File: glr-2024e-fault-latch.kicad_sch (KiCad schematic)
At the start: 110 parts, among them K101 Fujitsu_FTR-LYAA005x, K102 Fujitsu_FTR-LYAA005x, K103 Fujitsu_FTR-LYAA005x, Q101 Q_NPN_BEC, Q102 Q_NPN_BEC, Q103 Q_NPN_BEC, Q104 Q_NPN_BEC, Q105 Q_NMOS_GSD, Q106 Q_NMOS_GSD, Q107 Q_PMOS_GSD, Q108 Q_PMOS_GSD, Q109 Q_NMOS_GDS, Q110 Q_NPN_BEC, Q111 Q_NPN_BEC, Q112 Q_NMOS_GSD, Q113 Q_PMOS_GSD, Q114 Q_NMOS_GSD, Q115 Q_NMOS_GSD, SW101 SW_Omron_B3FS, SW102 SW_Omron_B3FS, SW103 SW_Omron_B3FS, U101 SFH617A-1, U102 SFH617A-1, U103 SFH617A-1, U104 74AHC1G00, U105 74AHC1G00, U106 74AHC1G00, U107 74LS279, U108 641964-1, U109 SFH617A-1, U110 SFH617A-1, U111 641964-1, U112 641964-1, U113 641964-1, U114 641964-1, U115 641964-1, U116 641964-1, U117 74AHC1G00, U118 LM555xM, U119 74AHC1G00, U120 641964-1, U121 SFH617A-1, U122 641964-1, U123 641964-1

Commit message: work in progress
keep only bms and imd
remove tssi stuff

Co-Authored-By: wallalex0 <97884125+wallalex0@users.noreply.github.com>
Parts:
- removed C104: 100n, Capacitor_SMD:C_0603_1608Metric_Pad1.08x0.95mm_HandSolder, symbol Device:C
- removed C106: 10n, Capacitor_SMD:C_0603_1608Metric_Pad1.08x0.95mm_HandSolder, symbol Device:C
- removed C107: 1u, Capacitor_SMD:C_0402_1005Metric, symbol Device:C_Polarized_US
- removed C108, C110, C112: 0.1u, Capacitor_SMD:C_0402_1005Metric, symbol Device:C
- removed C109: .01u, Capacitor_SMD:C_0402_1005Metric, symbol Device:C
- removed C111: 22u, Capacitor_SMD:C_0402_1005Metric, symbol Device:C
- removed D103: RED, LED_SMD:LED_0805_2012Metric_Pad1.15x1.40mm_HandSolder, symbol Device:LED
- removed D105, D107, D108: D_Schottky, Diode_SMD:D_SMA, symbol Device:D_Schottky
- removed K102: Fujitsu_FTR-LYAA005x, Relay_THT:Relay_SPST-NO_Fujitsu_FTR-LYAA005x_FormA_Vertical, symbol Relay:Fujitsu_FTR-LYAA005x
- removed Q109: Q_NMOS_GDS, Package_TO_SOT_SMD:TO-252-2, symbol Transistor_FET:Q_NMOS_GDS
- removed Q110, Q111: Q_NPN_BEC, Package_TO_SOT_SMD:SOT-23, symbol Transistor_BJT:Q_NPN_BEC
- removed Q112: Q_NMOS_GSD, Package_TO_SOT_SMD:SOT-23, symbol Transistor_FET:Q_NMOS_GSD
- removed Q113: Q_PMOS_GSD, Package_TO_SOT_SMD:SOT-523, symbol Transistor_FET:Q_PMOS_GSD
- removed R104, R107, R123: 10k, Resistor_SMD:R_0805_2012Metric_Pad1.20x1.40mm_HandSolder, symbol Device:R_US
- removed R118: 270R, Resistor_SMD:R_0805_2012Metric_Pad1.20x1.40mm_HandSolder, symbol Device:R_US
- removed R122, R127: 100k, Resistor_SMD:R_0805_2012Metric_Pad1.20x1.40mm_HandSolder, symbol Device:R_US
- removed R124, R129: 1k, Resistor_SMD:R_0805_2012Metric_Pad1.20x1.40mm_HandSolder, symbol Device:R_US
- removed R128, R133, R134: 10k, Resistor_SMD:R_0603_1608Metric, symbol Device:R_US
- removed R130: 270R, Resistor_SMD:R_0603_1608Metric, symbol Device:R_US
- removed R131: 15k, Resistor_SMD:R_0603_1608Metric, symbol Device:R_US
- removed R132: 100k, Resistor_SMD:R_0603_1608Metric, symbol Device:R_US
- removed SW103: SW_Omron_B3FS, Button_Switch_SMD:SW_SPST_Omron_B3FS-100xP, symbol Switch:SW_Omron_B3FS
- removed U103, U121: SFH617A-1, Package_DIP:DIP-4_W7.62mm, symbol Isolator:SFH617A-1
- removed U106, U117, U119: 74AHC1G00, Package_TO_SOT_SMD:SOT-23-5, symbol 74xGxx:74AHC1G00
- removed U111, U113, U114, U122: 641964-1, 641964-1:TE_641964-1, symbol CONNECTOR:641964-1
- removed U118: LM555xM, Package_SO:SOIC-8_3.9x4.9mm_P1.27mm, symbol Timer:LM555xM
- U101, U102, U107, U108, U109, U110, U112, U115, U116, U120, U123: now fitted
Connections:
- net +12V: no longer R102.2
- net GNDPWR: now also R102.1
- net BMS_INPUT: now reaches U101.1
- net BMS_INPUT: now also U115.1; no longer R102.1
- net SDC_IN: now reaches K103.13, U112.1
- net SDC: now reaches K103.14
- net SDC: now also K101.13; no longer U112.2
- net at U107.11 (~{S}): no longer U107.12 (~{S})
- net at U108.1: now also R112.2; no longer Q106.3 (D)
- net at U108.2: now also Q106.3 (D); no longer R112.2
- net SDC_OUT: now reaches K101.14
- net SDC_OUT: now also U112.2
- net at Q115.3 (D): now also U123.2; no longer U123.1
- net at R135.2: now also U123.1; no longer U123.2
- net BSPD_HV: no longer names the net of U116.2
- net IMD_HV renamed IMD_INPUT
- net NBMS_HV: no longer names the net of U101.2
- net NBMS_HV: now also R102.2; no longer U115.2
- net NBPSD_LV: no longer names the net of U107.10 (~{R})
- no-connect marks 5 -> 9
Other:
- note removed: "f = 1 / (0.693 * (2R106) * C102)"
- note removed: "https://www.electronics-tutorials.ws/waveforms/555_oscillator.html"
- moved on the sheet: C105, C113, C114, C115, C116, C117, D101, D106, H101, H102, H103, H104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

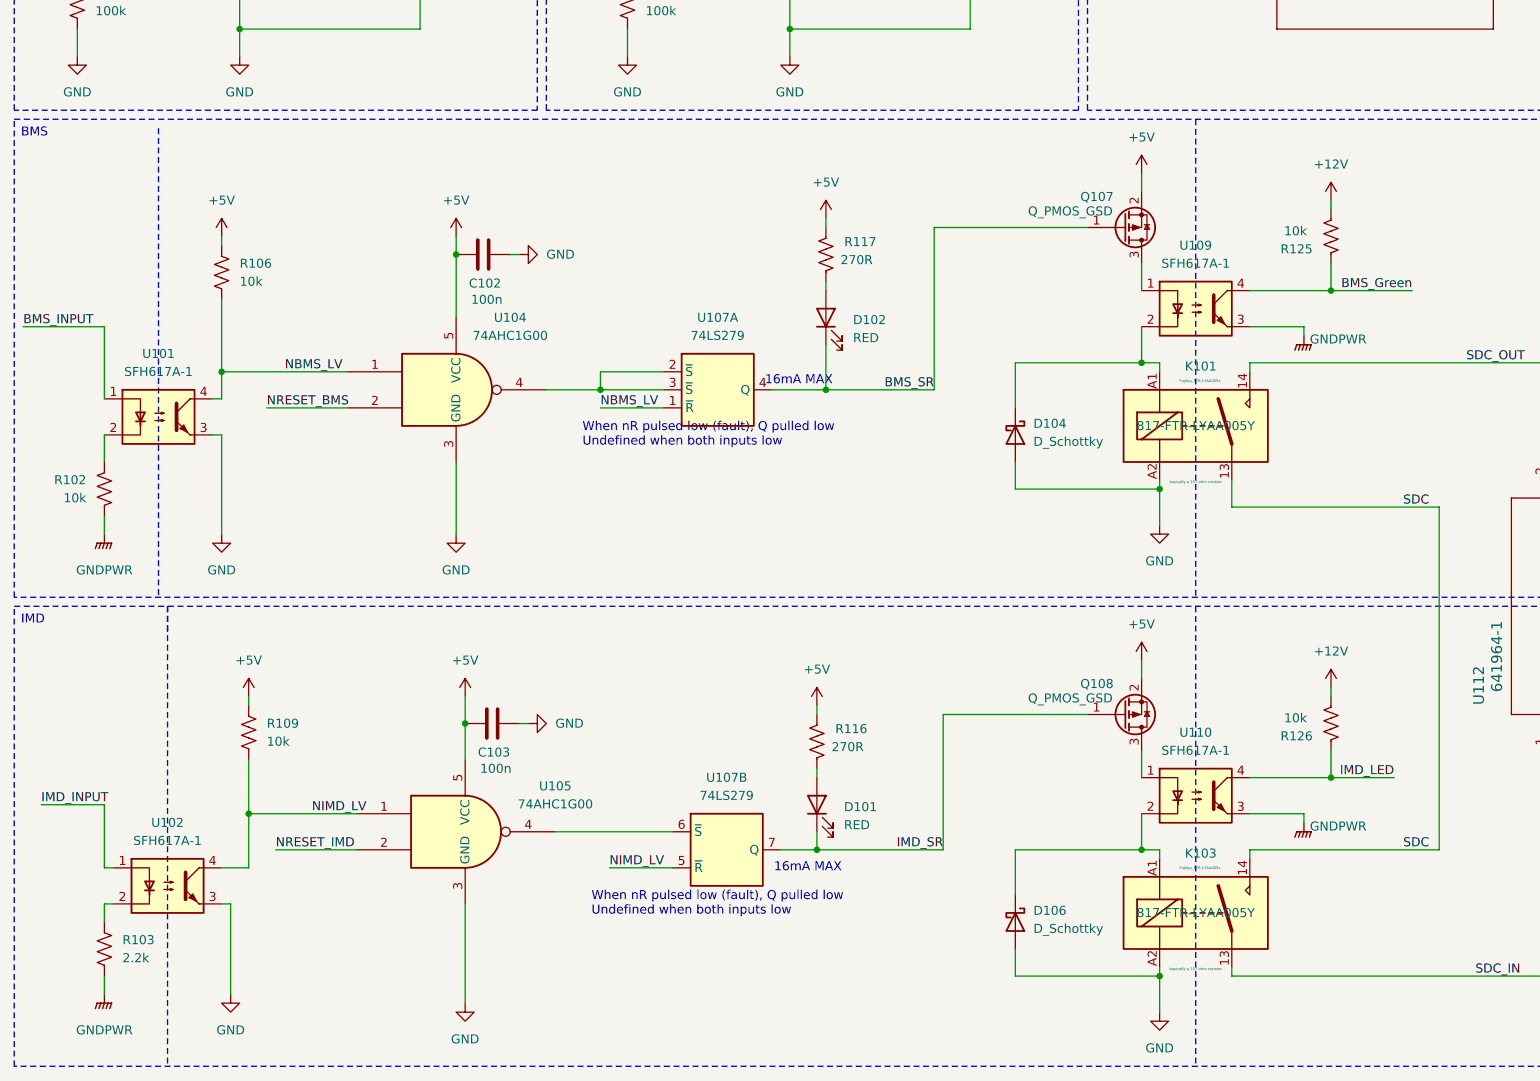
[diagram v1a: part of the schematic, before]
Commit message: almost finished
add bms light logic
improve overall placements of components
improve routing
improve silk component identifiers

Co-Authored-By: wallalex0 <97884125+wallalex0@users.noreply.github.com>
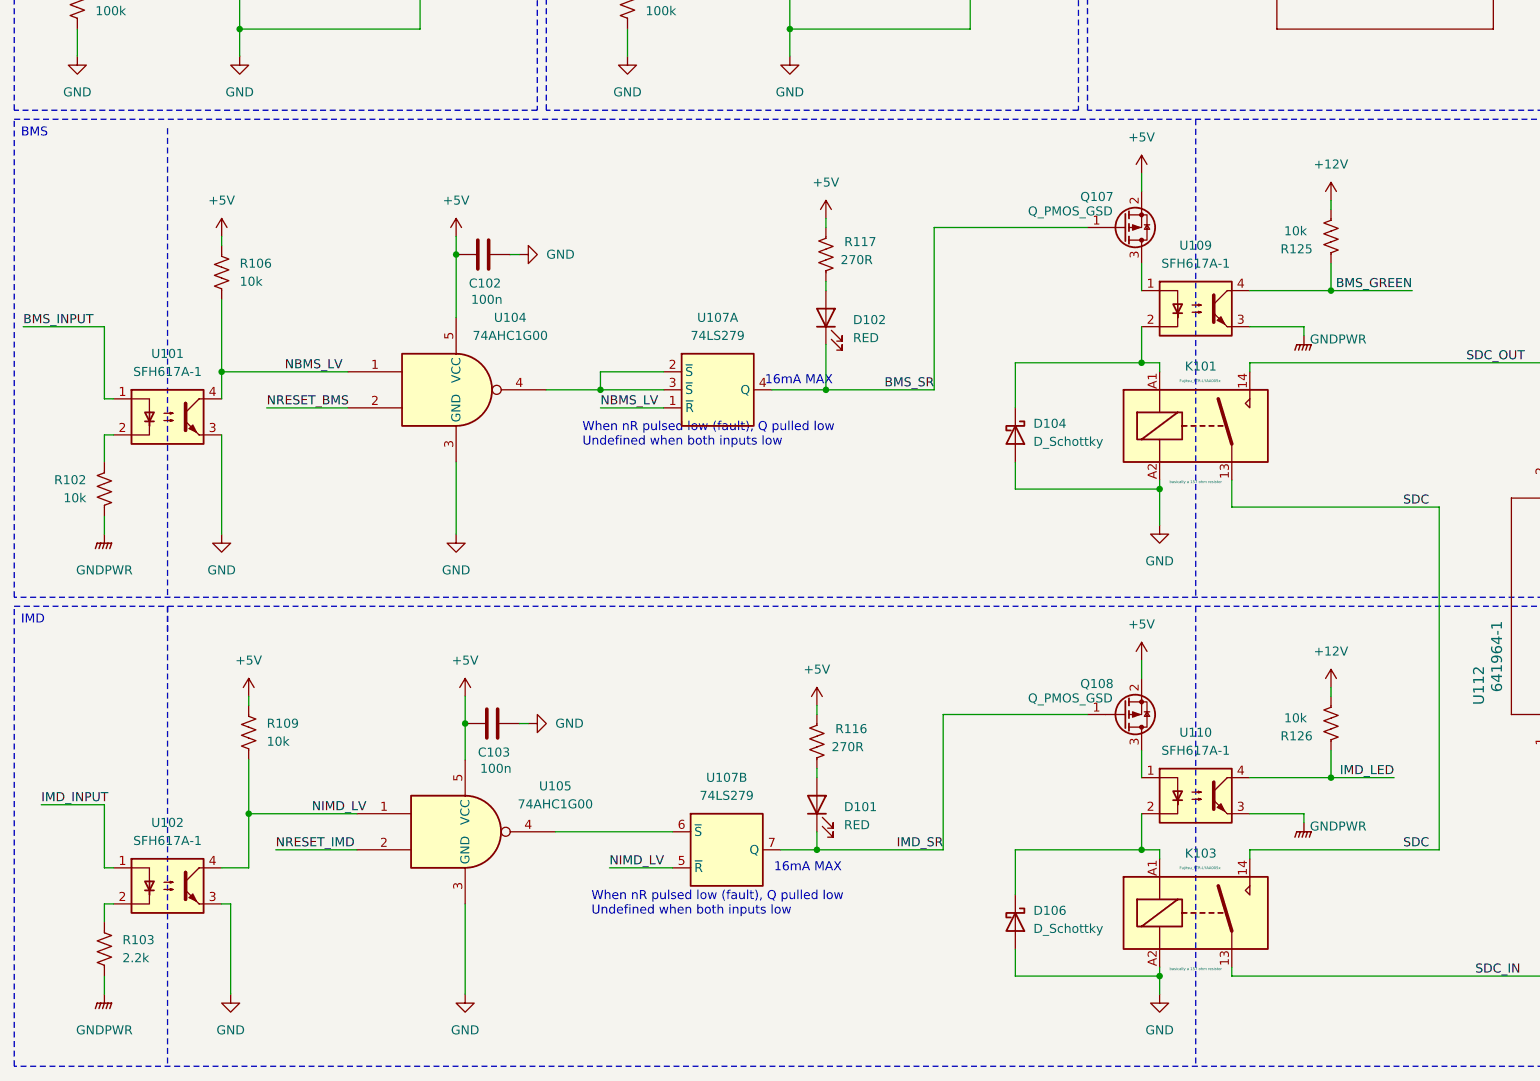
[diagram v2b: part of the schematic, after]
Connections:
- net BMS_Green is gone; now on net BMS_GREEN: R125.2, U109.4
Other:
- moved on the sheet: U101
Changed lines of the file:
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@@
 	(polyline
 		(pts
-			(xy 45.72 85.09) (xy 45.72 151.13)
+			(xy 46.99 85.09) (xy 46.99 151.13)
 		)
 		(stroke
@@
 	(wire
 		(pts
+			(xy 39.37 128.27) (xy 38.1 128.27)
+		)
+		(stroke
+			(width 0)
+			(type default)
+		)
+	)
+	(wire
+		(pts
 			(xy 308.61 125.73) (xy 308.61 115.57)
 		)
@@
 	(wire
 		(pts
-			(xy 53.34 128.27) (xy 54.61 128.27)
-		)
-		(stroke
-			(width 0)
-			(type default)
-		)
-	)
-	(wire
-		(pts
 			(xy 58.42 165.1) (xy 58.42 166.37)
 		)
@@
 	(wire
 		(pts
+			(xy 38.1 123.19) (xy 39.37 123.19)
+		)
+		(stroke
+			(width 0)
+			(type default)
+		)
+	)
+	(wire
+		(pts
 			(xy 276.86 113.03) (xy 288.29 113.03)
 		)
@@
 	(wire
 		(pts
-			(xy 186.69 204.47) (xy 186.69 209.55)
+			(xy 186.69 204.47) (xy 186.69 207.01)
 		)
 		(stroke
@@
 	(wire
 		(pts
+			(xy 38.1 128.27) (xy 38.1 132.08)
+		)
+		(stroke
+			(width 0)
+			(type default)
+		)
+	)
+	(wire
+		(pts
 			(xy 58.42 173.99) (xy 58.42 181.61)
 		)
@@
 	(wire
 		(pts
-			(xy 38.1 128.27) (xy 38.1 132.08)
-		)
-		(stroke
-			(width 0)
-			(type default)
-		)
-	)
-	(wire
-		(pts
 			(xy 156.21 167.64) (xy 176.53 167.64)
 		)
@@
 	(wire
 		(pts
-			(xy 54.61 123.19) (xy 53.34 123.19)
-		)
-		(stroke
-			(width 0)
-			(type default)
-		)
-	)
-	(wire
-		(pts
 			(xy 255.27 113.03) (xy 255.27 135.89)
 		)
@@
 	(wire
 		(pts
-			(xy 88.9 194.31) (xy 88.9 208.28)
+			(xy 88.9 194.31) (xy 88.9 207.01)
 		)
 		(stroke
@@
 		)
 	)
-	(label "BMS_Green"
+	(label "BMS_GREEN"
 		(at 222.25 107.95 180)
 		(effects
@@
 		(lib_name "GND_1")
 		(lib_id "power:GND")
-		(at 88.9 208.28 0)
+		(at 88.9 207.01 0)
 		(unit 1)
 		(exclude_from_sim no)
@@
 		(fields_autoplaced yes)
 		(property "Reference" "#PWR0119"
-			(at 88.9 214.63 0)
+			(at 88.9 213.36 0)
 			(effects
 				(font
@@
 		)
 		(property "Value" "GND"
-			(at 88.9 213.36 0)
+			(at 88.9 212.09 0)
 			(effects
 				(font
@@
 		)
 		(property "Footprint" ""
-			(at 88.9 208.28 0)
+			(at 88.9 207.01 0)
 			(effects
 				(font
@@
 		)
 		(property "Datasheet" ""
-			(at 88.9 208.28 0)
+			(at 88.9 207.01 0)
 			(effects
 				(font
@@
 		)
 		(property "Description" "Power symbol creates a global label with name \"GND\" , ground"
-			(at 88.9 208.28 0)
+			(at 88.9 207.01 0)
 			(effects
 				(font
@@
 	(symbol
 		(lib_id "Isolator:SFH617A-1")
-		(at 45.72 125.73 0)
+		(at 46.99 125.73 0)
 		(unit 1)
 		(exclude_from_sim no)
@@
 		(fields_autoplaced yes)
 		(property "Reference" "U101"
-			(at 45.72 116.84 0)
+			(at 46.99 116.84 0)
 			(effects
 				(font
@@
 		)
 		(property "Value" "SFH617A-1"
-			(at 45.72 119.38 0)
+			(at 46.99 119.38 0)
 			(effects
 				(font
@@
 		)
 		(property "Footprint" "Package_DIP:DIP-4_W7.62mm"
-			(at 40.64 130.81 0)
+			(at 41.91 130.81 0)
 			(effects
 				(font
@@
 		)
 		(property "Datasheet" "http://www.vishay.com/docs/83740/sfh617a.pdf"
-			(at 45.72 125.73 0)
+			(at 46.99 125.73 0)
 			(effects
 				(font
@@
 		)
 		(property "Description" "Optocoupler, Phototransistor Output, 5300 VRMS, VCEO 70V, CTR% 40-80, -55 to +110 degree Celsius, UL, BSI, FIMKO, cUL, THT PDIP-4"
-			(at 45.72 125.73 0)
+			(at 46.99 125.73 0)
 			(effects
 				(font
@@
 		)
 		(property "JLC#" ""
-			(at 45.72 125.73 0)
+			(at 46.99 125.73 0)
 			(effects
 				(font
@@
 		)
 		(property "Sim.Device" ""
-			(at 45.72 125.73 0)
+			(at 46.99 125.73 0)
 			(effects
 				(font
@@
 		)
 		(property "Sim.Pins" ""
-			(at 45.72 125.73 0)
+			(at 46.99 125.73 0)
 			(effects
 				(font
@@
 		)
 		(property "Sim.Type" ""
-			(at 45.72 125.73 0)
+			(at 46.99 125.73 0)
 			(effects
 				(font
@@
 		)
 		(property "MOUSER" "SFH617A-1X007T "
-			(at 45.72 125.73 0)
+			(at 46.99 125.73 0)
 			(effects
 				(font
@@
 		)
 		(property "Notes" ""
-			(at 45.72 125.73 0)
+			(at 46.99 125.73 0)
 			(effects
 				(font
@@
 					(size 1.27 1.27)
 				)
+				(hide yes)
 			)
 		)
@@
 					(size 1.27 1.27)
 				)
+				(hide yes)
 			)
 		)
@@
 		(lib_name "GND_1")
 		(lib_id "power:GND")
-		(at 186.69 209.55 0)
+		(at 186.69 207.01 0)
 		(unit 1)
 		(exclude_from_sim no)
@@
 		(fields_autoplaced yes)
 		(property "Reference" "#PWR0145"
-			(at 186.69 215.9 0)
+			(at 186.69 213.36 0)
 			(effects
 				(font
@@
 		)
 		(property "Value" "GND"
-			(at 186.69 214.63 0)
+			(at 186.69 212.09 0)
 			(effects
 				(font
@@
 		)
 		(property "Footprint" ""
-			(at 186.69 209.55 0)
+			(at 186.69 207.01 0)
 			(effects
 				(font
@@
 		)
 		(property "Datasheet" ""
-			(at 186.69 209.55 0)
+			(at 186.69 207.01 0)
 			(effects
 				(font
@@
 		)
 		(property "Description" "Power symbol creates a global label with name \"GND\" , ground"
-			(at 186.69 209.55 0)
+			(at 186.69 207.01 0)
 			(effects
 				(font

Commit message: add details
add license

Co-Authored-By: wallalex0 <97884125+wallalex0@users.noreply.github.com>
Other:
- company: (none) -> Green Lion Racing
- title: (none) -> Fault latch for IMD and BMS/AMS
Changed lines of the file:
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@@
 	(generator_version "9.0")
 	(paper "A2")
+	(title_block
+		(title "Fault latch for IMD and BMS/AMS")
+		(date "2025-06-13")
+		(rev "v3")
+		(company "Green Lion Racing")
+		(comment 1 "Alexander Wallrodt")
+	)
 	(text "12V"
 		(exclude_from_sim no)
